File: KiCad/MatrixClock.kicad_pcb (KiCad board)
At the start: 2 copper layers, 160 x 32 mm, 36 parts, among them J1 FDTI 3.3V, J2 USB_OTG, J3 CONN_01X05, J4 CONN_01X05, J5 DISP_PWR, M1 Module_MAX7219, M2 Module_MAX7219, M3 Module_MAX7219, M4 Module_MAX7219, M5 Module_MAX7219, Q1 BC557, SW1 SW_Push, U1 BME280, U2 APDS-9301, U3 ESP-12E, U4 LD1117S33TR, U5 BME680

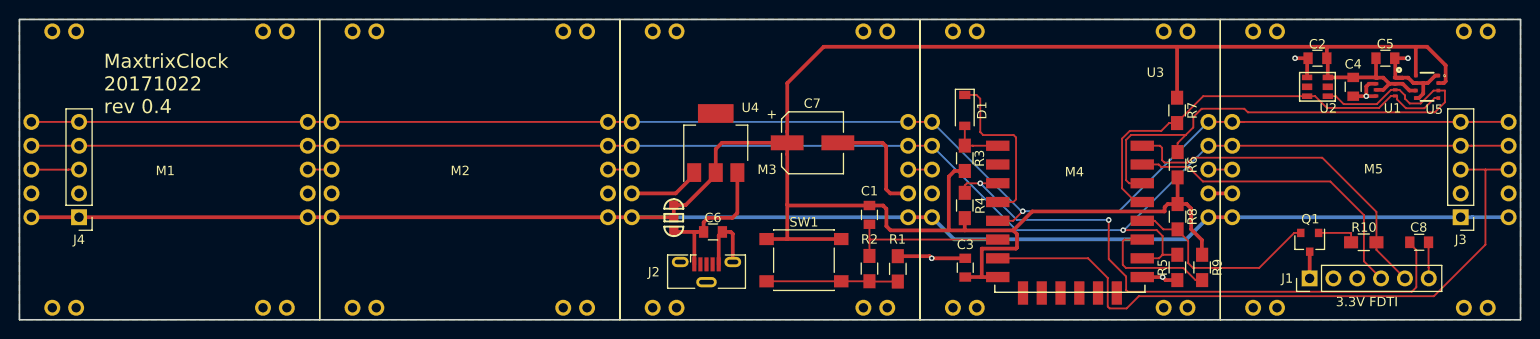
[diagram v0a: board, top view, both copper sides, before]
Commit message: Bumped version to 0.5
Features:
* Reworked the matrix module layout, the 2 header pins where 0.4mm off.
* Added BH1750FVI as an alternative light sensor.

Fixed issues:
* R10 should be connected to RX, not TX (seen from ESP12, not FTDI connector)
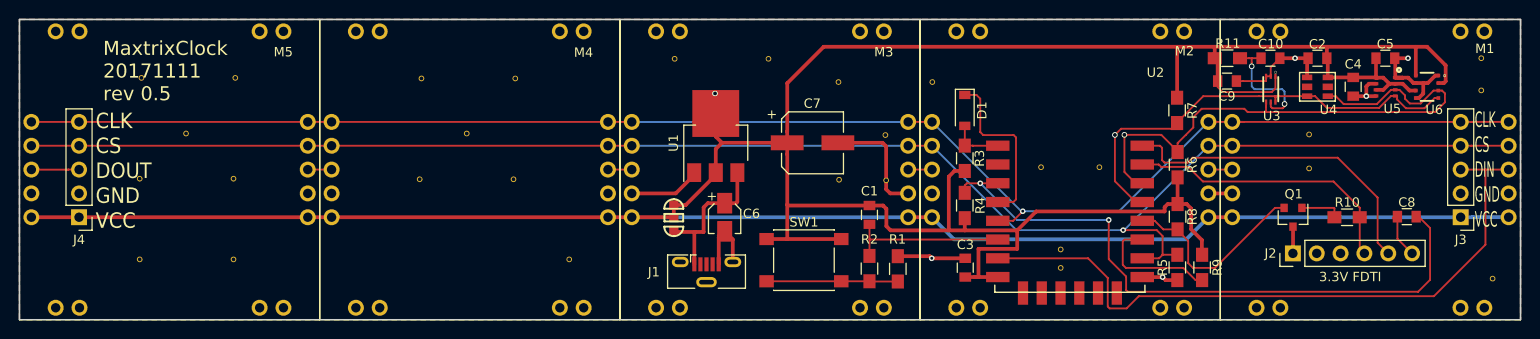
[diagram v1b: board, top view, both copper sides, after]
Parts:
- removed the U4 at (101.2, 33.2)
- added C10: 100nF, Capacitors_SMD:C_0805, F.Cu at (160.3, 24.1)
- added C9: 100nF, Capacitors_SMD:C_0805, F.Cu at (155.7, 26.6)
- added R11: 1K, Resistors_SMD:R_0805_HandSoldering, F.Cu at (155.8, 24.1)
- added U1: LD1117S33TR, TO_SOT_Packages_SMD:SOT-223-3Lead_TabPin2, F.Cu at (101.2, 33.2)
- added U3: BH1750FVI-TR, Private:WSOF6, F.Cu at (160.4, 27.4)
- added VIA01: VIA-6mm, Private:VIA-6mm, F.Cu at (119.3, 32.3)
- added VIA02: VIA-6mm, Private:VIA-6mm, F.Cu at (114.4, 37.1)
- added VIA03: VIA-6mm, Private:VIA-6mm, F.Cu at (119.4, 37.1)
- added VIA04: VIA-6mm, Private:VIA-6mm, F.Cu at (124.3, 26.7)
- added VIA05: VIA-6mm, Private:VIA-6mm, F.Cu at (114.3, 26.7)
- added VIA06: VIA-6mm, Private:VIA-6mm, F.Cu at (106.8, 24.2)
- added VIA07: VIA-6mm, Private:VIA-6mm, F.Cu at (96.8, 24.2)
- added VIA07: VIA-6mm, Private:VIA-6mm, F.Cu at (184.0, 47.6)
- added VIA08: VIA-6mm, Private:VIA-6mm, F.Cu at (138.0, 46.5)
- added VIA09: VIA-6mm, Private:VIA-6mm, F.Cu at (138.0, 44.5)
- added VIA10: VIA-6mm, Private:VIA-6mm, F.Cu at (142.1, 35.8)
- added VIA11: VIA-6mm, Private:VIA-6mm, F.Cu at (135.9, 35.8)
- added VIA12: VIA-6mm, Private:VIA-6mm, F.Cu at (164.5, 35.9)
- added VIA13: VIA-6mm, Private:VIA-6mm, F.Cu at (182.8, 24.1)
- added VIA14: VIA-6mm, Private:VIA-6mm, F.Cu at (182.8, 27.6)
- added VIA15: VIA-6mm, Private:VIA-6mm, F.Cu at (164.5, 32.3)
- added VIA17: VIA-6mm, Private:VIA-6mm, F.Cu at (79.7, 37.0)
- added VIA20: VIA-6mm, Private:VIA-6mm, F.Cu at (69.7, 37.0)
- added VIA21: VIA-6mm, Private:VIA-6mm, F.Cu at (69.8, 26.3)
- added VIA22: VIA-6mm, Private:VIA-6mm, F.Cu at (79.8, 26.3)
- added VIA23: VIA-6mm, Private:VIA-6mm, F.Cu at (85.6, 45.6)
- added VIA23: VIA-6mm, Private:VIA-6mm, F.Cu at (49.8, 45.6)
- added VIA24: VIA-6mm, Private:VIA-6mm, F.Cu at (49.8, 37.0)
- added VIA26: VIA-6mm, Private:VIA-6mm, F.Cu at (39.8, 45.6)
- added VIA26: VIA-6mm, Private:VIA-6mm, F.Cu at (39.8, 37.0)
- added VIA27: VIA-6mm, Private:VIA-6mm, F.Cu at (44.8, 32.2)
- added VIA28: VIA-6mm, Private:VIA-6mm, F.Cu at (50.0, 26.2)
- added VIA29: VIA-6mm, Private:VIA-6mm, F.Cu at (40.0, 26.2)
- added VIA31: VIA-6mm, Private:VIA-6mm, F.Cu at (74.7, 32.2)
- C3: value 10nF -> 100nF
- C6: value 10nF -> 10uF; footprint Capacitors_SMD:C_0805 -> Capacitors_SMD:CP_Elec_3x5.3
- J2: renamed from J1; value FDTI 3.3V -> CONN_01X06
- Q1: value BC557 -> PNP
- moved J2 3.21 mm to (162.7, 44.9)
- moved Q1 3.21 mm to (162.8, 41.1)
- moved R10 3.21 mm to (168.5, 41.1)
- moved C8 3.03 mm to (174.9, 41.0), turned to 0 degrees
- moved C6 2.00 mm to (102.2, 41.1), turned to 270 degrees
- renumbered J2 to J1, M5 to M1, M4 to M2, M2 to M4, M1 to M5, U3 to U2, U2 to U4, U1 to U5, U5 to U6
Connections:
- J1 pad 2: Net-(J2-Pad2) -> (no net)
- J1 pad 3: Net-(J2-Pad3) -> (no net)
- J1 pad 4: Net-(J2-Pad4) -> (no net)
- J2 pad 2: Net-(J1-Pad2) -> (no net)
- J2 pad 3: Net-(J1-Pad3) -> (no net)
- R10 pad 1: /TxD -> /RxD
- U2 pad 17: Net-(U3-Pad17) -> (no net)
- U2 pad 18: Net-(U3-Pad18) -> (no net)
- U2 pad 19: Net-(U3-Pad19) -> (no net)
- U2 pad 2: Net-(U3-Pad2) -> (no net)
- U2 pad 20: Net-(U3-Pad20) -> (no net)
- U2 pad 21: Net-(U3-Pad21) -> (no net)
- U2 pad 22: Net-(U3-Pad22) -> (no net)
- U4 pad 3: Net-(U2-Pad3) -> (no net)
- U4 pad 6: Net-(U2-Pad6) -> (no net)
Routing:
- net +3V3: track 220.5 -> 236.4 mm, vias 0 -> 1
- net Net-(C10-Pad2): track 0.00 -> 12.9 mm, vias 0 -> 2
- net GND: track 64.6 -> 72.9 mm
- net /CH_PD: track 64.9 -> 69.2 mm
- net /RxD: track 34.1 -> 31.6 mm
- net /TxD: track 38.1 -> 35.7 mm
- net /SCL: track 45.3 -> 47.2 mm, vias 0 -> 1
- net /SDA: track 60.5 -> 61.4 mm, vias 0 -> 1
- net /DTR: track 3.86 -> 4.68 mm
- net /GPIO0: track 22.7 -> 22.0 mm
- added copper zone on F.Cu, net GND
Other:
- board text added: "CLK CS DIN GND VCC"
- board text added: "CLK CS DOUT GND VCC"
- board text added: "MaxtrixClock 20171111 rev 0.5"
- board text removed: "MaxtrixClock 20171022 rev 0.4"
